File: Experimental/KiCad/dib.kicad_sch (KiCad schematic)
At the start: 7 parts, among them X10 10018783-10101TLF, X11 77313-802-20LF, X12 77313-802-20LF, X13 10018783-10101TLF, X14 5051102091, X15 TBP03R1-350-10BE

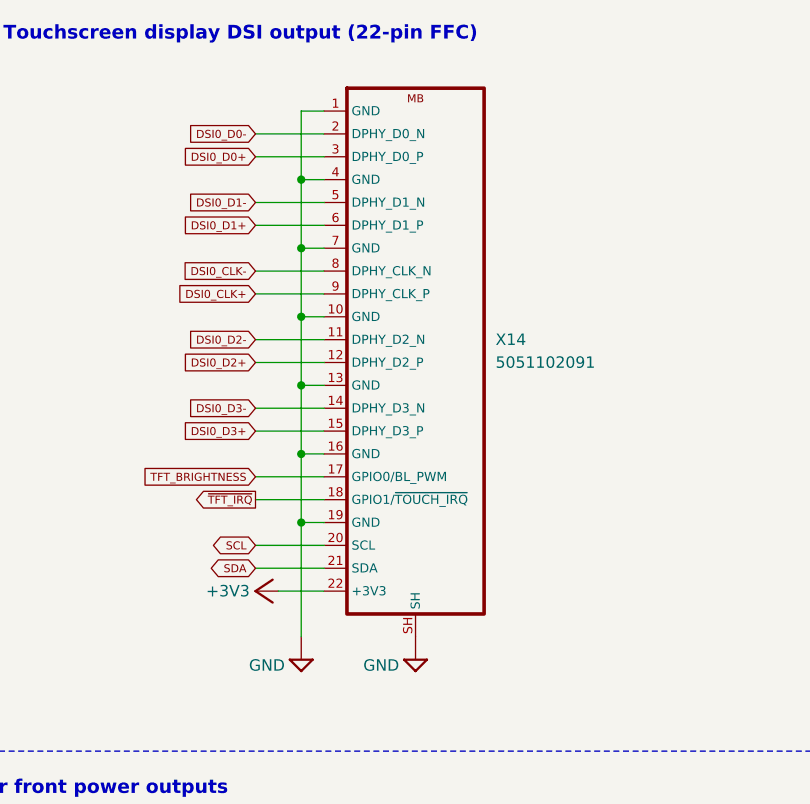
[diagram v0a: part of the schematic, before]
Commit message: BOM update, small changes
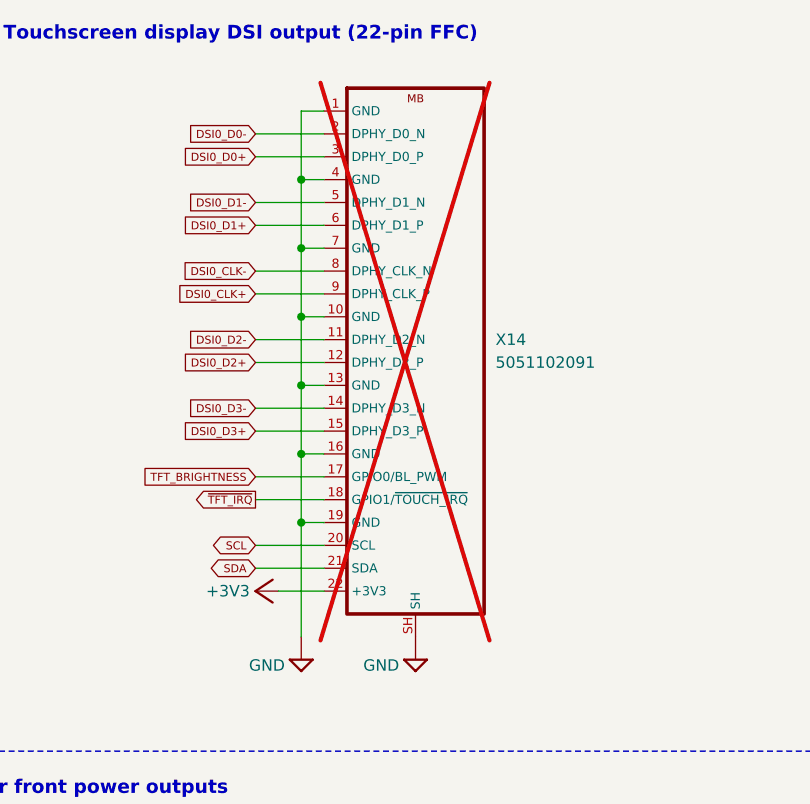
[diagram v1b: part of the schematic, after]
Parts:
- X14: now not fitted; now left out of the parts list
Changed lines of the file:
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@@
 	(title_block
 		(title "BB3+ test mainboard")
-		(date "2025-10-11")
+		(date "2025-10-12")
 		(rev "r1B1")
 		(company "Envox d.o.o.")
@@
 		(on_board yes)
 		(dnp no)
-		(property "Reference" "#SUPPLY057"
+		(property "Reference" "#SUPPLY058"
 			(at 81.28 109.22 0)
 			(effects
@@
 			(project "BB3plus MCU test board"
 				(path "/1df84e4f-233a-4f72-9418-c0020706bb76/57aee854-8c94-4105-bcce-97e3d73b363b"
-					(reference "#SUPPLY057")
+					(reference "#SUPPLY058")
 					(unit 1)
 				)
@@
 		(on_board yes)
 		(dnp no)
-		(property "Reference" "#SUPPLY060"
+		(property "Reference" "#SUPPLY061"
 			(at 157.48 109.22 0)
 			(effects
@@
 			(project "BB3plus MCU test board"
 				(path "/1df84e4f-233a-4f72-9418-c0020706bb76/57aee854-8c94-4105-bcce-97e3d73b363b"
-					(reference "#SUPPLY060")
+					(reference "#SUPPLY061")
 					(unit 1)
 				)
@@
 		(unit 1)
 		(exclude_from_sim no)
-		(in_bom yes)
+		(in_bom no)
 		(on_board yes)
-		(dnp no)
+		(dnp yes)
 		(fields_autoplaced yes)
 		(property "Reference" "X14"
@@
 		(on_board yes)
 		(dnp no)
-		(property "Reference" "#SUPPLY059"
+		(property "Reference" "#SUPPLY060"
 			(at 119.38 50.8 0)
 			(effects
@@
 			(project "BB3plus MCU test board"
 				(path "/1df84e4f-233a-4f72-9418-c0020706bb76/57aee854-8c94-4105-bcce-97e3d73b363b"
-					(reference "#SUPPLY059")
+					(reference "#SUPPLY060")
 					(unit 1)
 				)
@@
 		(on_board yes)
 		(dnp no)
-		(property "Reference" "#SUPPLY058"
+		(property "Reference" "#SUPPLY059"
 			(at 83.82 50.8 0)
 			(effects
@@
 			(project "BB3plus MCU test board"
 				(path "/1df84e4f-233a-4f72-9418-c0020706bb76/57aee854-8c94-4105-bcce-97e3d73b363b"
-					(reference "#SUPPLY058")
+					(reference "#SUPPLY059")
 					(unit 1)
 				)
@@
 		(on_board yes)
 		(dnp no)
-		(property "Reference" "#SUPPLY061"
+		(property "Reference" "#SUPPLY062"
 			(at 160.02 50.8 0)
 			(effects
@@
 			(project "BB3plus MCU test board"
 				(path "/1df84e4f-233a-4f72-9418-c0020706bb76/57aee854-8c94-4105-bcce-97e3d73b363b"
-					(reference "#SUPPLY061")
+					(reference "#SUPPLY062")
 					(unit 1)
 				)
@@
 		(on_board yes)
 		(dnp no)
-		(property "Reference" "#SUPPLY056"
+		(property "Reference" "#SUPPLY057"
 			(at 43.18 50.8 0)
 			(effects
@@
 			(project "BB3plus MCU test board"
 				(path "/1df84e4f-233a-4f72-9418-c0020706bb76/57aee854-8c94-4105-bcce-97e3d73b363b"
-					(reference "#SUPPLY056")
+					(reference "#SUPPLY057")
 					(unit 1)
 				)

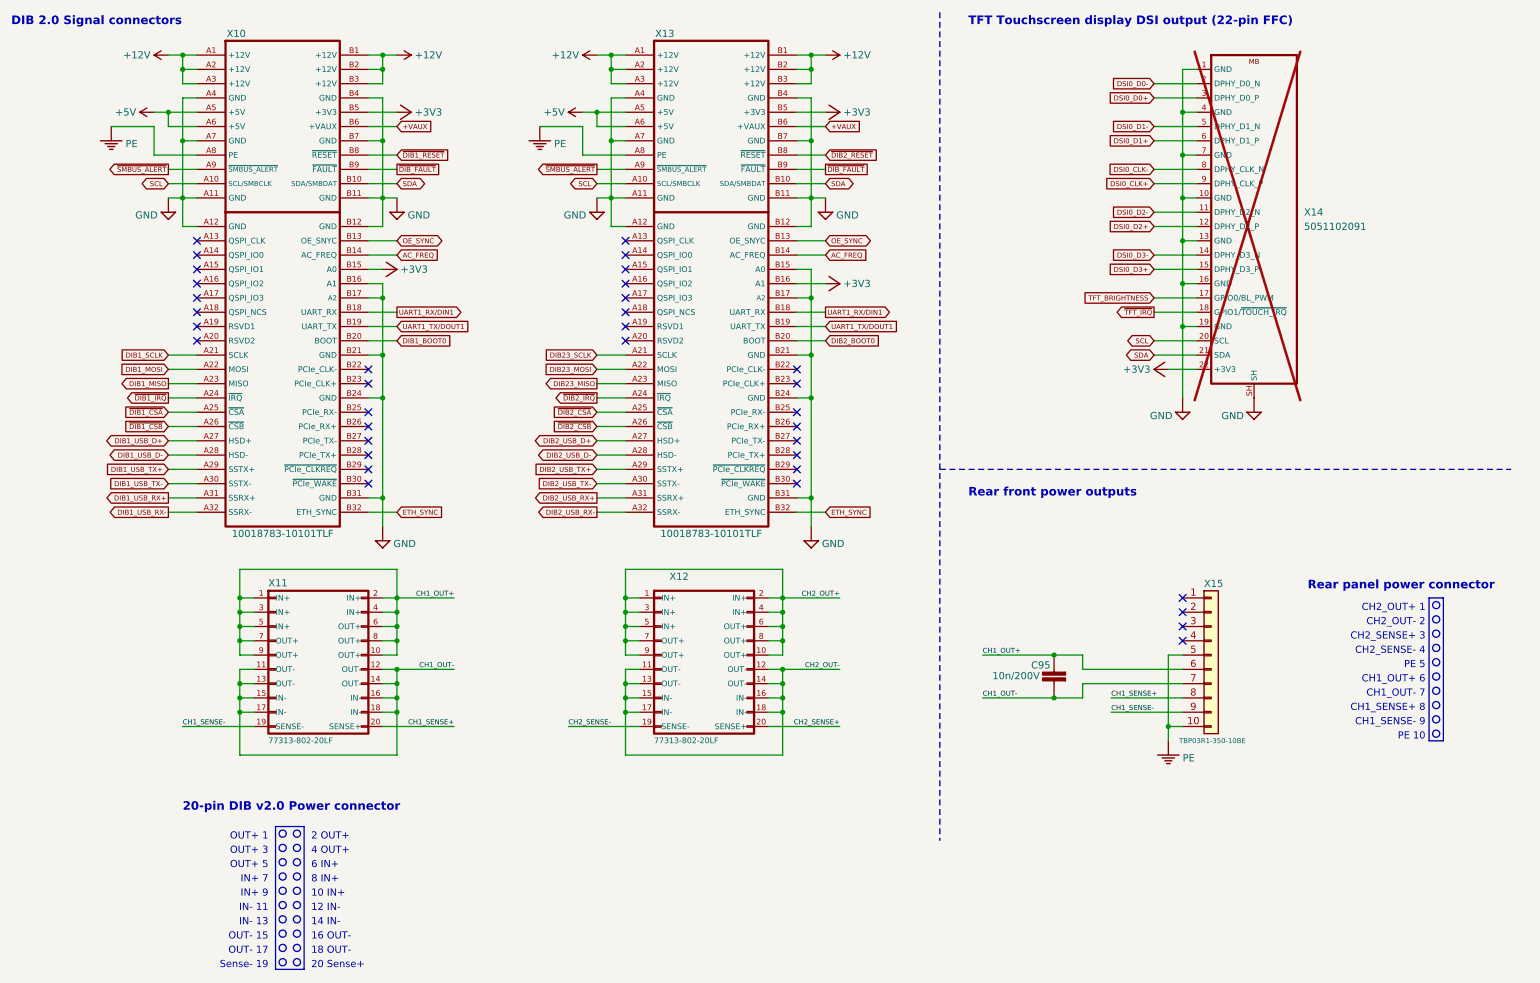
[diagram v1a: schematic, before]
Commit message: Replace 5V buck with 6A low EMI version
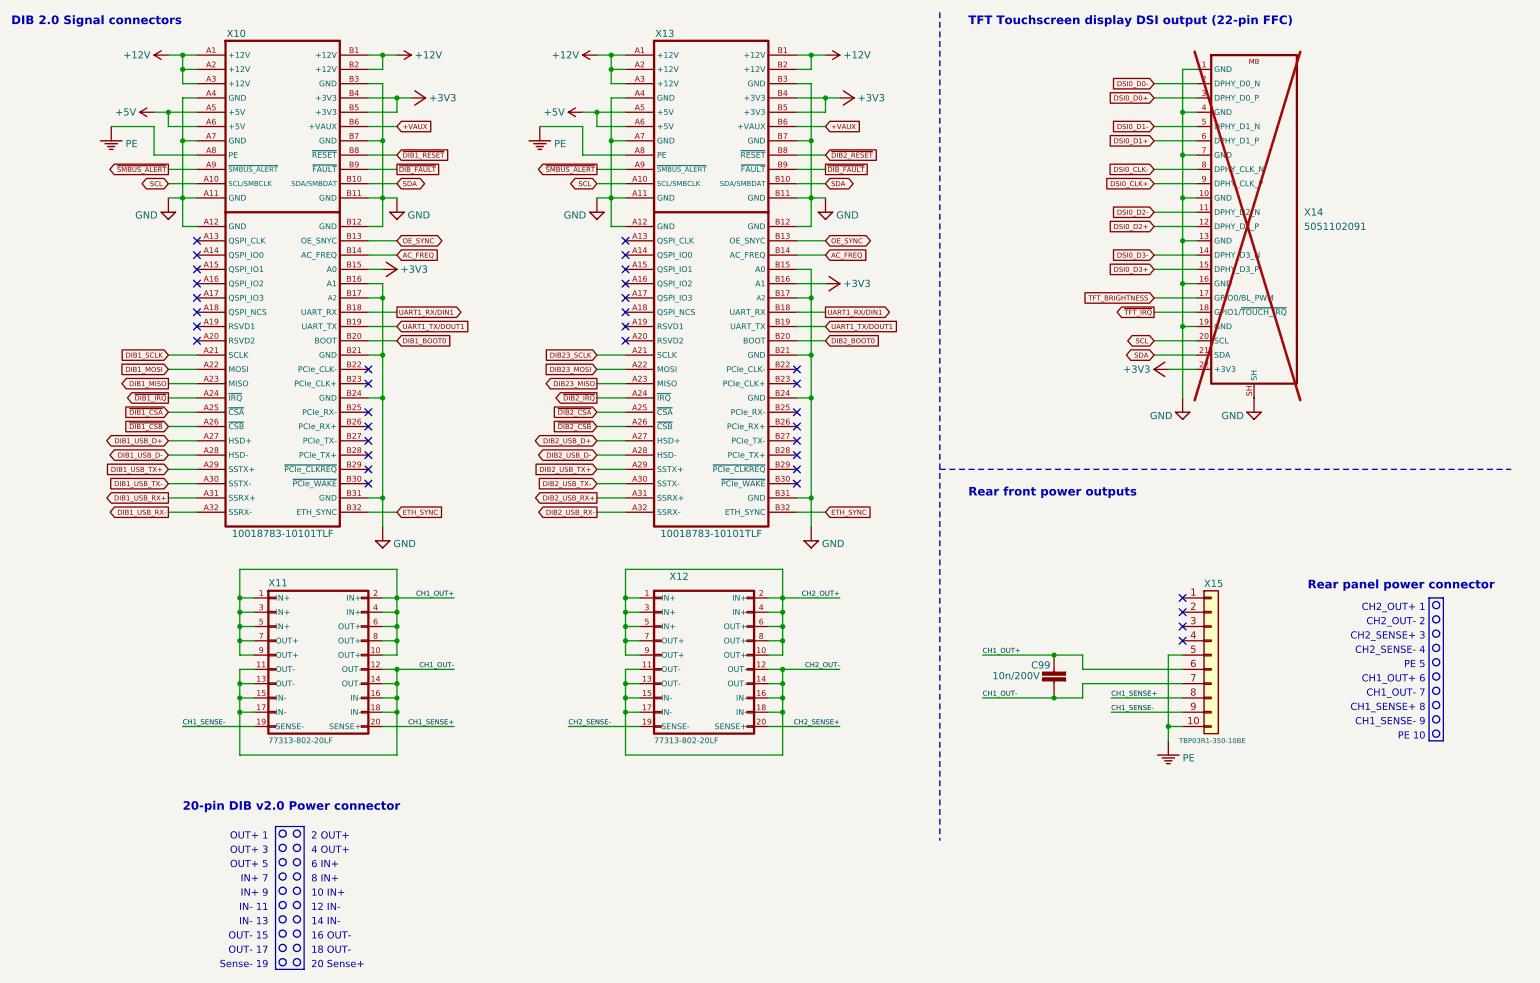
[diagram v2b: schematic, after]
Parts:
- renumbered C95 to C99
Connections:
- net +12V: no longer X10.B3 (+12V), X13.B3 (+12V)
- net +3V3: now also X10.B4 (+3V3), X13.B4 (+3V3)
- net GND: now also X10.B3 (GND), X13.B3 (GND); no longer X10.B4 (GND), X13.B4 (GND)
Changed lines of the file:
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@@
 	)
 	(junction
+		(at 83.82 30.48)
+		(diameter 0)
+		(color 0 0 0 0)
+	)
+	(junction
 		(at 55.88 137.16)
 		(diameter 0)
@@
 	)
 	(junction
-		(at 81.28 25.4)
-		(diameter 0)
-		(color 0 0 0 0)
-	)
-	(junction
 		(at 83.82 132.08)
 		(diameter 0)
@@
 	)
 	(junction
-		(at 83.82 137.16)
+		(at 160.02 30.48)
 		(diameter 0)
 		(color 0 0 0 0)
 	)
 	(junction
-		(at 200.66 129.54)
+		(at 83.82 137.16)
 		(diameter 0)
 		(color 0 0 0 0)
 	)
 	(junction
-		(at 55.88 139.7)
+		(at 200.66 129.54)
 		(diameter 0)
 		(color 0 0 0 0)
 	)
 	(junction
-		(at 45.72 22.86)
+		(at 55.88 139.7)
 		(diameter 0)
 		(color 0 0 0 0)
 	)
 	(junction
-		(at 157.48 25.4)
+		(at 45.72 22.86)
 		(diameter 0)
 		(color 0 0 0 0)
@@
 	(wire
 		(pts
+			(xy 78.74 30.48) (xy 83.82 30.48)
+		)
+		(stroke
+			(width 0)
+			(type default)
+		)
+	)
+	(wire
+		(pts
 			(xy 149.86 137.16) (xy 152.4 137.16)
 		)
@@
 	(wire
 		(pts
-			(xy 157.48 30.48) (xy 157.48 38.1)
+			(xy 152.4 114.3) (xy 152.4 119.38)
 		)
 		(stroke
@@
 	(wire
 		(pts
-			(xy 152.4 114.3) (xy 152.4 119.38)
+			(xy 154.94 66.04) (xy 157.48 66.04)
 		)
 		(stroke
@@
 	(wire
 		(pts
-			(xy 154.94 66.04) (xy 157.48 66.04)
+			(xy 154.94 30.48) (xy 160.02 30.48)
 		)
 		(stroke
@@
 	(wire
 		(pts
+			(xy 83.82 30.48) (xy 83.82 33.02)
+		)
+		(stroke
+			(width 0)
+			(type default)
+		)
+	)
+	(wire
+		(pts
 			(xy 81.28 101.6) (xy 81.28 83.82)
 		)
@@
 	(wire
 		(pts
+			(xy 160.02 30.48) (xy 162.56 30.48)
+		)
+		(stroke
+			(width 0)
+			(type default)
+		)
+	)
+	(wire
+		(pts
 			(xy 78.74 33.02) (xy 83.82 33.02)
 		)
@@
 	(wire
 		(pts
-			(xy 154.94 27.94) (xy 157.48 27.94)
+			(xy 83.82 30.48) (xy 86.36 30.48)
 		)
 		(stroke
@@
 	(wire
 		(pts
-			(xy 55.88 134.62) (xy 55.88 137.16)
+			(xy 154.94 27.94) (xy 157.48 27.94)
 		)
 		(stroke
@@
 	(wire
 		(pts
-			(xy 223.52 48.26) (xy 226.06 48.26)
+			(xy 55.88 134.62) (xy 55.88 137.16)
 		)
 		(stroke
@@
 	(wire
 		(pts
-			(xy 78.74 63.5) (xy 81.28 63.5)
+			(xy 223.52 48.26) (xy 226.06 48.26)
 		)
 		(stroke
@@
 	(wire
 		(pts
-			(xy 157.48 25.4) (xy 157.48 27.94)
+			(xy 78.74 63.5) (xy 81.28 63.5)
 		)
 		(stroke
@@
 	(wire
 		(pts
-			(xy 81.28 30.48) (xy 81.28 38.1)
+			(xy 81.28 27.94) (xy 81.28 38.1)
 		)
 		(stroke
@@
 	(wire
 		(pts
-			(xy 81.28 25.4) (xy 81.28 27.94)
-		)
-		(stroke
-			(width 0)
-			(type default)
-		)
-	)
-	(wire
-		(pts
 			(xy 119.38 35.56) (xy 124.46 35.56)
 		)
@@
 	(wire
 		(pts
+			(xy 157.48 27.94) (xy 157.48 38.1)
+		)
+		(stroke
+			(width 0)
+			(type default)
+		)
+	)
+	(wire
+		(pts
 			(xy 149.86 134.62) (xy 152.4 134.62)
 		)
@@
 	(wire
 		(pts
-			(xy 78.74 30.48) (xy 81.28 30.48)
+			(xy 160.02 30.48) (xy 160.02 33.02)
 		)
 		(stroke
@@
 	(wire
 		(pts
-			(xy 154.94 30.48) (xy 157.48 30.48)
-		)
-		(stroke
-			(width 0)
-			(type default)
-		)
-	)
-	(wire
-		(pts
 			(xy 81.28 66.04) (xy 81.28 76.2)
 		)
@@
 		(on_board yes)
 		(dnp no)
-		(property "Reference" "#SUPPLY058"
+		(property "Reference" "#SUPPLY060"
 			(at 81.28 109.22 0)
 			(effects
@@
 			(project "BB3plus MCU test board"
 				(path "/1df84e4f-233a-4f72-9418-c0020706bb76/57aee854-8c94-4105-bcce-97e3d73b363b"
-					(reference "#SUPPLY058")
+					(reference "#SUPPLY060")
 					(unit 1)
 				)
@@
 		(on_board yes)
 		(dnp no)
-		(property "Reference" "#SUPPLY061"
+		(property "Reference" "#SUPPLY063"
 			(at 157.48 109.22 0)
 			(effects
@@
 			(project "BB3plus MCU test board"
 				(path "/1df84e4f-233a-4f72-9418-c0020706bb76/57aee854-8c94-4105-bcce-97e3d73b363b"
-					(reference "#SUPPLY061")
+					(reference "#SUPPLY063")
 					(unit 1)
 				)
@@
 		(on_board yes)
 		(dnp no)
-		(property "Reference" "C95"
+		(property "Reference" "C99"
 			(at 200.025 132.08 0)
 			(effects
@@
 			(project "BB3plus MCU test board"
 				(path "/1df84e4f-233a-4f72-9418-c0020706bb76/57aee854-8c94-4105-bcce-97e3d73b363b"
-					(reference "C95")
+					(reference "C99")
 					(unit 1)
 				)
@@
 		(on_board yes)
 		(dnp no)
-		(property "Reference" "#SUPPLY060"
+		(property "Reference" "#SUPPLY062"
 			(at 119.38 50.8 0)
 			(effects
@@
 			(project "BB3plus MCU test board"
 				(path "/1df84e4f-233a-4f72-9418-c0020706bb76/57aee854-8c94-4105-bcce-97e3d73b363b"
-					(reference "#SUPPLY060")
+					(reference "#SUPPLY062")
 					(unit 1)
 				)
@@
 		(on_board yes)
 		(dnp no)
-		(property "Reference" "#SUPPLY059"
+		(property "Reference" "#SUPPLY061"
 			(at 83.82 50.8 0)
 			(effects
@@
 			(project "BB3plus MCU test board"
 				(path "/1df84e4f-233a-4f72-9418-c0020706bb76/57aee854-8c94-4105-bcce-97e3d73b363b"
-					(reference "#SUPPLY059")
+					(reference "#SUPPLY061")
 					(unit 1)
 				)
@@
 	(symbol
 		(lib_id "PCM_EEZ_symbols:+3V3")
-		(at 162.56 33.02 270)
+		(at 165.1 30.48 270)
 		(unit 1)
 		(exclude_from_sim no)
@@
 		(on_board yes)
 		(dnp no)
-		(property "Reference" "#+3V029"
-			(at 162.56 33.02 0)
+		(property "Reference" "#+3V030"
+			(at 165.1 30.48 0)
 			(effects
 				(font
@@
 		)
 		(property "Value" "+3V3"
-			(at 163.195 33.02 90)
+			(at 165.735 30.48 90)
 			(effects
 				(font
@@
 		)
 		(property "Footprint" ""
-			(at 162.56 33.02 0)
+			(at 165.1 30.48 0)
 			(effects
 				(font
@@
 		)
 		(property "Datasheet" ""
-			(at 162.56 33.02 0)
+			(at 165.1 30.48 0)
 			(effects
 				(font
@@
 		)
 		(property "Description" ""
-			(at 162.56 33.02 0)
+			(at 165.1 30.48 0)
 			(effects
 				(font
@@
 			(project "BB3plus MCU test board"
 				(path "/1df84e4f-233a-4f72-9418-c0020706bb76/57aee854-8c94-4105-bcce-97e3d73b363b"
-					(reference "#+3V029")
+					(reference "#+3V030")
 					(unit 1)
 				)
@@
 		(on_board yes)
 		(dnp no)
-		(property "Reference" "#+3V030"
+		(property "Reference" "#+3V029"
 			(at 162.56 63.5 0)
 			(effects
@@
 			(project "BB3plus MCU test board"
 				(path "/1df84e4f-233a-4f72-9418-c0020706bb76/57aee854-8c94-4105-bcce-97e3d73b363b"
-					(reference "#+3V030")
+					(reference "#+3V029")
 					(unit 1)
 				)
@@
 		(on_board yes)
 		(dnp no)
-		(property "Reference" "#SUPPLY062"
+		(property "Reference" "#SUPPLY064"
 			(at 160.02 50.8 0)
 			(effects
@@
 			(project "BB3plus MCU test board"
 				(path "/1df84e4f-233a-4f72-9418-c0020706bb76/57aee854-8c94-4105-bcce-97e3d73b363b"
-					(reference "#SUPPLY062")
+					(reference "#SUPPLY064")
 					(unit 1)
 				)
@@
 	(symbol
 		(lib_id "PCM_EEZ_symbols:+3V3")
-		(at 86.36 33.02 270)
+		(at 88.9 30.48 270)
 		(unit 1)
 		(exclude_from_sim no)
@@
 		(dnp no)
 		(property "Reference" "#+3V028"
-			(at 86.36 33.02 0)
+			(at 88.9 30.48 0)
 			(effects
 				(font
@@
 		)
 		(property "Value" "+3V3"
-			(at 86.995 33.02 90)
+			(at 89.535 30.48 90)
 			(effects
 				(font
@@
 		)
 		(property "Footprint" ""
-			(at 86.36 33.02 0)
+			(at 88.9 30.48 0)
 			(effects
 				(font
@@
 		)
 		(property "Datasheet" ""
-			(at 86.36 33.02 0)
+			(at 88.9 30.48 0)
 			(effects
 				(font
@@
 		)
 		(property "Description" ""
-			(at 86.36 33.02 0)
+			(at 88.9 30.48 0)
 			(effects
 				(font
@@
 		(on_board yes)
 		(dnp no)
-		(property "Reference" "#SUPPLY057"
+		(property "Reference" "#SUPPLY059"
 			(at 43.18 50.8 0)
 			(effects
@@
 			(project "BB3plus MCU test board"
 				(path "/1df84e4f-233a-4f72-9418-c0020706bb76/57aee854-8c94-4105-bcce-97e3d73b363b"
-					(reference "#SUPPLY057")
+					(reference "#SUPPLY059")
 					(unit 1)
 				)

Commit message: Update project info
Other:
- company: Envox d.o.o. -> ${project_creator}
- title: BB3+ test mainboard -> ${project_name}
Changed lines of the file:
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@@
 	(paper "A4")
 	(title_block
-		(title "BB3+ test mainboard")
-		(date "2025-10-12")
-		(rev "r1B1")
-		(company "Envox d.o.o.")
-		(comment 1 "Licensed under the TAPR Open Hardware License (www.tapr.org/OHL)")
-		(comment 2 "More info at http://www.envox.eu/")
+		(title "${project_name}")
+		(date "2025-10-13")
+		(rev "${project_version}")
+		(company "${project_creator}")
+		(comment 1 "${project_license}")
+		(comment 2 "${project_info}")
 	)
 	(circle

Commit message: Output LC filters added on all buck converters
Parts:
- renumbered C99 to C102
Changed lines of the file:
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@@
 	(title_block
 		(title "${project_name}")
-		(date "2025-10-13")
+		(date "2025-10-14")
 		(rev "${project_version}")
 		(company "${project_creator}")
@@
 		(on_board yes)
 		(dnp no)
-		(property "Reference" "#SUPPLY060"
+		(property "Reference" "#SUPPLY063"
 			(at 81.28 109.22 0)
 			(effects
@@
 			(project "BB3plus MCU test board"
 				(path "/1df84e4f-233a-4f72-9418-c0020706bb76/57aee854-8c94-4105-bcce-97e3d73b363b"
-					(reference "#SUPPLY060")
+					(reference "#SUPPLY063")
 					(unit 1)
 				)
@@
 		(on_board yes)
 		(dnp no)
-		(property "Reference" "#SUPPLY063"
+		(property "Reference" "#SUPPLY066"
 			(at 157.48 109.22 0)
 			(effects
@@
 			(project "BB3plus MCU test board"
 				(path "/1df84e4f-233a-4f72-9418-c0020706bb76/57aee854-8c94-4105-bcce-97e3d73b363b"
-					(reference "#SUPPLY063")
+					(reference "#SUPPLY066")
 					(unit 1)
 				)
@@
 		(on_board yes)
 		(dnp no)
-		(property "Reference" "C99"
+		(property "Reference" "C102"
 			(at 200.025 132.08 0)
 			(effects
@@
 			(project "BB3plus MCU test board"
 				(path "/1df84e4f-233a-4f72-9418-c0020706bb76/57aee854-8c94-4105-bcce-97e3d73b363b"
-					(reference "C99")
+					(reference "C102")
 					(unit 1)
 				)
@@
 		(on_board yes)
 		(dnp no)
-		(property "Reference" "#SUPPLY062"
+		(property "Reference" "#SUPPLY065"
 			(at 119.38 50.8 0)
 			(effects
@@
 			(project "BB3plus MCU test board"
 				(path "/1df84e4f-233a-4f72-9418-c0020706bb76/57aee854-8c94-4105-bcce-97e3d73b363b"
-					(reference "#SUPPLY062")
+					(reference "#SUPPLY065")
 					(unit 1)
 				)
@@
 		(on_board yes)
 		(dnp no)
-		(property "Reference" "#SUPPLY061"
+		(property "Reference" "#SUPPLY064"
 			(at 83.82 50.8 0)
 			(effects
@@
 			(project "BB3plus MCU test board"
 				(path "/1df84e4f-233a-4f72-9418-c0020706bb76/57aee854-8c94-4105-bcce-97e3d73b363b"
-					(reference "#SUPPLY061")
+					(reference "#SUPPLY064")
 					(unit 1)
 				)
@@
 		(on_board yes)
 		(dnp no)
-		(property "Reference" "#SUPPLY064"
+		(property "Reference" "#SUPPLY067"
 			(at 160.02 50.8 0)
 			(effects
@@
 			(project "BB3plus MCU test board"
 				(path "/1df84e4f-233a-4f72-9418-c0020706bb76/57aee854-8c94-4105-bcce-97e3d73b363b"
-					(reference "#SUPPLY064")
+					(reference "#SUPPLY067")
 					(unit 1)
 				)
@@
 		(on_board yes)
 		(dnp no)
-		(property "Reference" "#SUPPLY059"
+		(property "Reference" "#SUPPLY062"
 			(at 43.18 50.8 0)
 			(effects
@@
 			(project "BB3plus MCU test board"
 				(path "/1df84e4f-233a-4f72-9418-c0020706bb76/57aee854-8c94-4105-bcce-97e3d73b363b"
-					(reference "#SUPPLY059")
+					(reference "#SUPPLY062")
 					(unit 1)
 				)
